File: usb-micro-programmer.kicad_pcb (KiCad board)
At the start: 2 copper layers, 60 x 30 mm, 38 parts, among them J1 USB_B_Micro, J2 ESP_Link, J3 ESP_Prog, J4 Standard_Prog, Q1 S8050(NPN), Q2 S8050(NPN), U1 CH340C/G, U2 AMS1117-3.3, Y1 12MHz

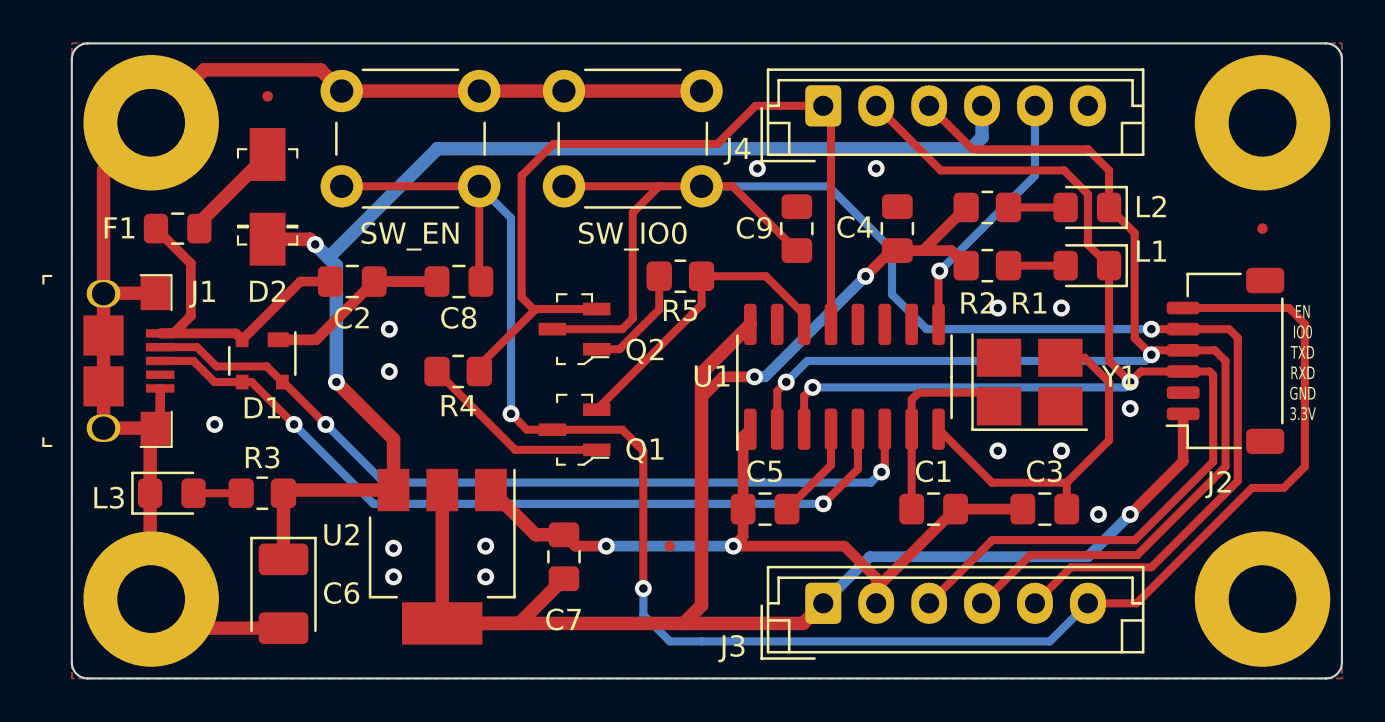
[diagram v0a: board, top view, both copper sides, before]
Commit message: Correcting changes based on gerbers
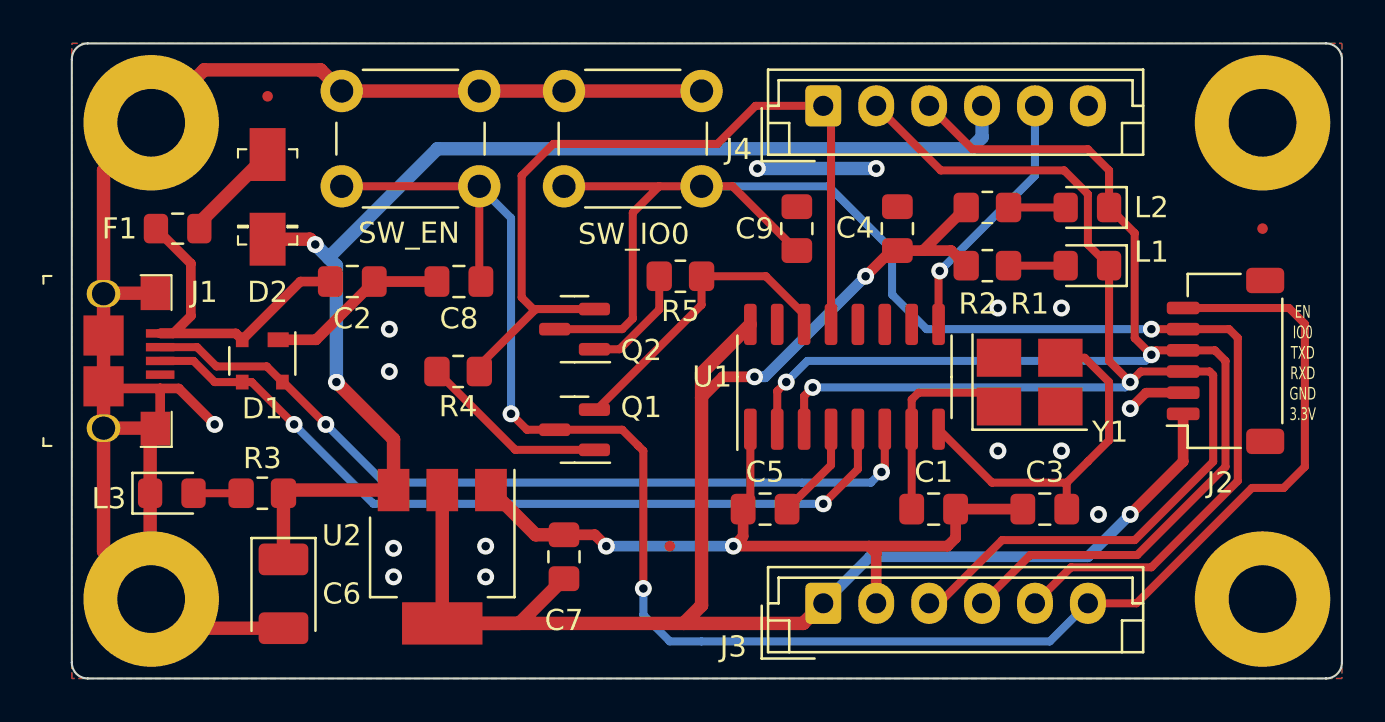
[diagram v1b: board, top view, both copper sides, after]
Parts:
- C7: value 22uF/10V -> 22uF/25V
- C8, C9: value 0.1uF/25V -> 0.1uF
- Q1, Q2: footprint digikey-footprints:SOT-23-3 -> Package_TO_SOT_SMD:SOT-23
- R1, R2: value 1K(5%) -> 1K
- R3: value 2K(5%) -> 2K
- R4, R5: value 10k(5%) -> 10k
- SW_EN, SW_IO0: footprint Button_Switch_THT:SW_PUSH_6mm_H9.5mm -> Button_Switch_THT:SW_PUSH_6mm_H5mm
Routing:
- net GND: track 109.5 -> 133.2 mm
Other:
- board text added: "ESP USB Micro Prog Rev 0.1.2 (210422)"
- board text removed: "ESP USB Micro Prog V 0.1.2 (210422)"

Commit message: Adding changes of Rev 0.1.4
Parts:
- moved J2 1.66 mm to (137.2, 105.0)
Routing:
- net GND: track 133.2 -> 139.4 mm
- net /EN: track 85.1 -> 79.5 mm, vias 2 -> 3
- net /IO0: track 71.3 -> 73.8 mm
- net /RXD: track 63.2 -> 65.6 mm
- net /TXD: track 62.5 -> 64.9 mm
- net +3V3: track 87.3 -> 88.0 mm
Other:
- board text added: "ESP USB Micro Prog Rev 0.1.4 (210422)"
- board text removed: "ESP USB Micro Prog Rev 0.1.2 (210422)"
